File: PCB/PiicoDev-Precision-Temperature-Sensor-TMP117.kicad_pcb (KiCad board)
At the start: 2 copper layers, 25.4 x 25.4 mm, 23 parts, among them J1 , J2 , J3 , U1 TMP117

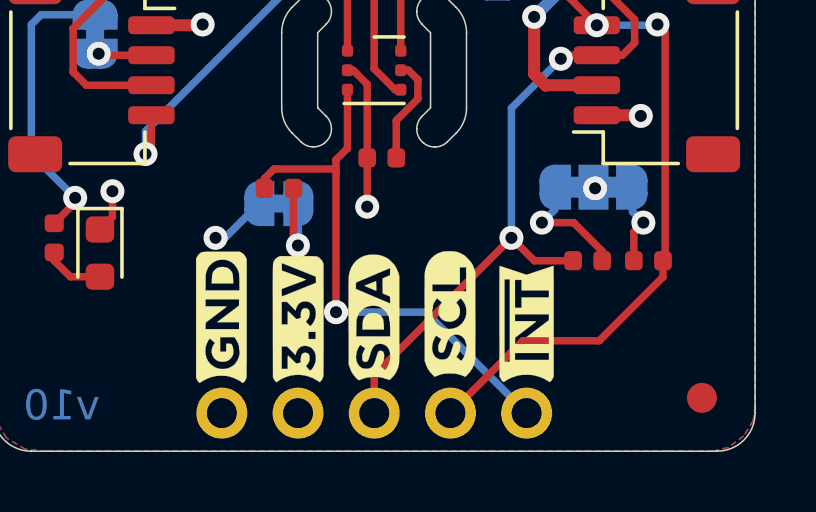
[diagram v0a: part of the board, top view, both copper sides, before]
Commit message: Update R1 to 4k7
New LED is more efficient, use larger resistor. Optimise 1k out of the BOM
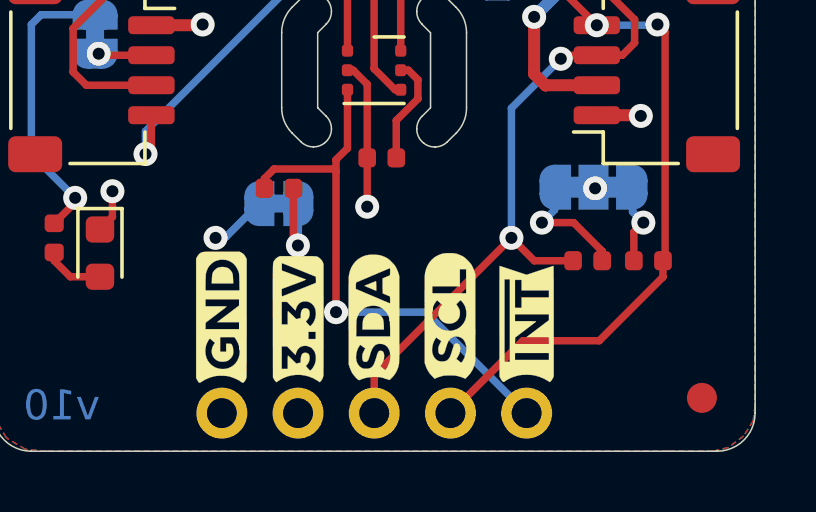
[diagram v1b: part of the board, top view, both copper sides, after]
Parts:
- R1: value 1k -> 4k7

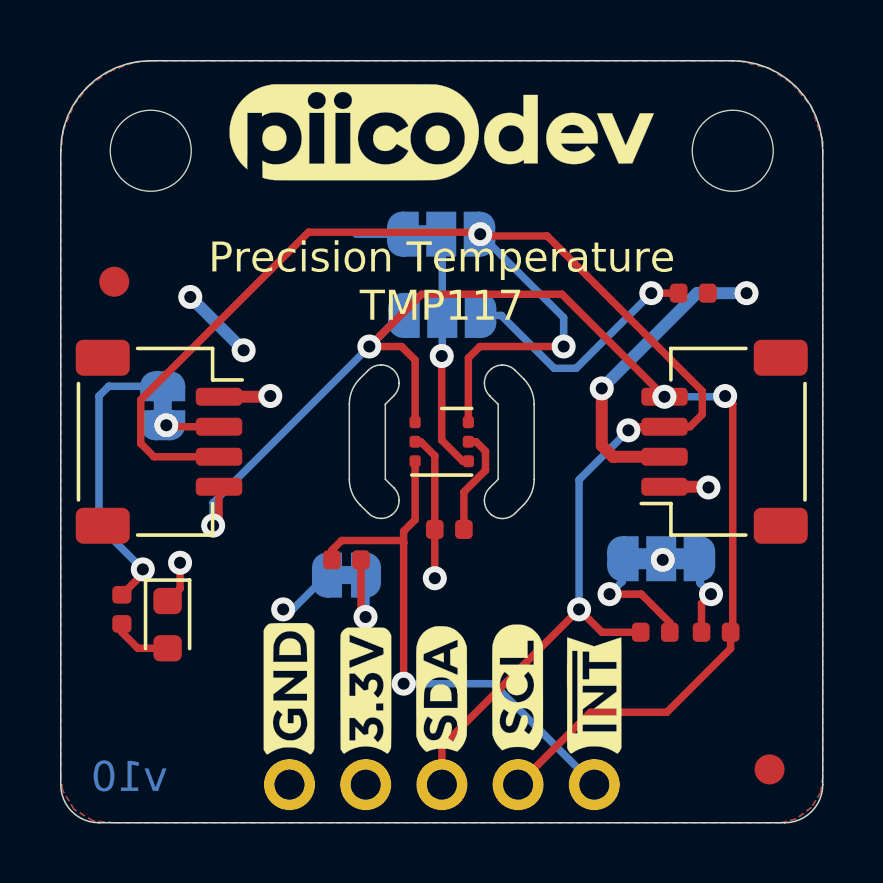
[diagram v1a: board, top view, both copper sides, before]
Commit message: v11 Update
Change resistor values
Add DIP switch and remove ADR jumper
Update graphic labels
Remove solder mask between jumper pads
Update text formatting
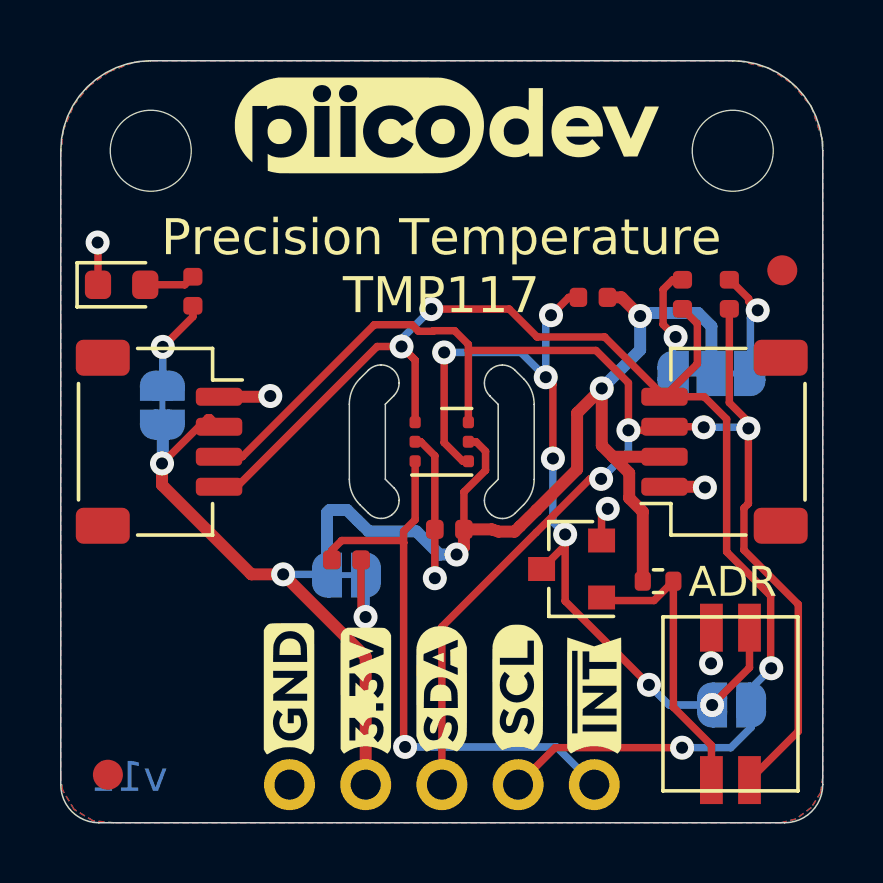
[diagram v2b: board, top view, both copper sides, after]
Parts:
- removed JP5: , Jumper:SolderJumper-3_P1.3mm_Bridged12_RoundedPad1.0x1.5mm
- added G3: LOGO_made-with-love, CoreElectronics_Artwork:piicodev_logo_14.2x3.4mm, B.Cu at (12.6, 2.27)
- added Q1: BSS138, Package_TO_SOT_SMD:SOT-23, F.Cu at (17.0, 16.9)
- added R6: 10k, Resistor_SMD:R_0402_1005Metric, F.Cu at (19.9, 17.3)
- added SW1: SW_DIP_x02, CoreElectronics_Components:SW_DIP_x02_Slide_CHS-02A1, F.Cu at (22.3, 21.4)
- G1: value LOGO_CoreElectronics_made-with-love -> LOGO_CoreElectronics_no-text; footprint PiicoDev_Artwork:piicodev_logo_14.2x3.4mm -> CoreElectronics_Artwork:CoreElectronics_logo_5mm
- G2: footprint Piico_Artwork:piicodev_logo_14.2x3.4mm -> CoreElectronics_Artwork:piicodev_logo_14.2x3.4mm
- JP1, JP2: footprint Jumper:SolderJumper-2_P1.3mm_Bridged_RoundedPad1.0x1.5mm -> CoreElectronics_Components:SolderJumper-2_P1.3mm_Bridged_RoundedPad1.0x1.5mm
- JP4: value (none) -> SolderJumper_2_Open; footprint Jumper:SolderJumper-3_P1.3mm_Open_RoundedPad1.0x1.5mm -> CoreElectronics_Components:SolderJumper-2_P1.3mm_Open_RoundedPad1.0x1.5mm
- R1, R3, R4: value 4k7 -> 10k
- moved FID1 22.3 mm to (24.1, 6.99)
- moved FID2 22.1 mm to (1.57, 23.8)
- moved G1 19.4 mm to (3.46, 19.6)
- moved JP4 16.2 mm to (22.4, 21.5), turned to 0 degrees
- moved R4 11.5 mm to (22.3, 7.79), turned to 270 degrees
- moved D1 11.4 mm to (2.03, 7.47), turned to 0 degrees
- moved R3 11.3 mm to (20.7, 7.79), turned to 270 degrees
- moved R1 10.9 mm to (4.40, 7.68), turned to 90 degrees
- moved LOGO1 6.42 mm to (22.4, 16.5)
- moved JP3 6.40 mm to (21.7, 10.4), turned to 180 degrees
- moved R5 3.35 mm to (17.7, 7.89)
- moved G2 0.29 mm to (12.9, 2.26)
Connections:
- JP4 pad 1: Net-(JP4-Pad1) -> /ADD0
- JP4 pad 2: /ADD0 -> /SCL
- R5 pad 2: Net-(JP4-Pad1) -> /ADD0
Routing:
- net +3V3: track 20.1 -> 56.0 mm, vias 7 -> 5
- net /ADD0: track 8.07 -> 29.9 mm, vias 1 -> 7
- net Net-(Q1-Pad1): track 0.00 -> 9.86 mm
- net Net-(JP4-Pad1): track 8.35 -> 0.00 mm, vias 1 -> 0
- net Net-(JP1-Pad2): track 9.78 -> 3.10 mm
- net /SDA: track 58.1 -> 56.7 mm
- net /SCL: track 46.4 -> 47.7 mm
- net /~INT: track 18.2 -> 19.4 mm
- net Net-(JP3-Pad3): track 2.73 -> 3.80 mm
- net GND: track 11.1 -> 11.8 mm, vias 4 -> 6
- added copper zone on F.Cu, net (none)
- removed copper zone on F.Cu, net +3V3
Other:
- net class +3V3 added: clearance 0.2, trace_width 0.4, via_dia 0.8, via_drill 0.4
- board text added: "ADR"
- board text added: "ADR3"
- board text added: "v11"
- board text removed: "48"
- board text removed: "49"
- board text removed: "4A"
- board text removed: "4B"
- board text removed: "ADDR"
- board text removed: "v10"

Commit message: v12 Update
Migrate to KiCad 6.0
Add 120R resistor
Add 4-bit DIP SW
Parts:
- removed JP4: SolderJumper_2_Open, CoreElectronics_Components:SolderJumper-2_P1.3mm_Open_RoundedPad1.0x1.5mm
- removed Q1: BSS138, Package_TO_SOT_SMD:SOT-23
- R6: value 10k -> 120R
- SW1: value SW_DIP_x02 -> SW_DIP_x04; footprint CoreElectronics_Components:SW_DIP_x02_Slide_CHS-02A1 -> CoreElectronics_Components:SW_DIP_x04_Slide_CHS-04A1
- moved G1 17.5 mm to (20.9, 21.3)
- moved R6 9.69 mm to (14.0, 9.65)
- moved R5 9.14 mm to (17.3, 17.0)
- moved J3 2.50 mm to (5.13, 24.1)
- moved SW1 1.46 mm to (20.9, 21.6)
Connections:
- net /~INT renamed /~{INT}
- R5 pad 2: /ADD0 -> Net-(SW1-Pad2)
- R6 pad 1: +3V3 -> Net-(R6-Pad1)
- R6 pad 2: Net-(Q1-Pad1) -> /SDA
- SW1 pad 1: Net-(Q1-Pad1) -> GND
- SW1 pad 2: /SDA -> Net-(SW1-Pad2)
- SW1 pad 3: /ADD0 -> Net-(R6-Pad1)
- SW1 pad 4: GND -> /SCL
- U1 pad 4: /ADD0 -> Net-(SW1-Pad5)
- U1 pad 6: /SDA -> Net-(R6-Pad1)
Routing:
- net /ADD0: track 29.9 -> 0.00 mm, vias 7 -> 0
- net Net-(R6-Pad1): track 0.00 -> 24.7 mm, vias 0 -> 4
- net Net-(SW1-Pad5): track 0.00 -> 22.7 mm, vias 0 -> 4
- net /SDA: track 56.7 -> 44.2 mm
- net Net-(Q1-Pad1): track 9.86 -> 0.00 mm
- net Net-(SW1-Pad2): track 0.00 -> 8.53 mm, vias 0 -> 2
- net /SCL: track 47.7 -> 56.2 mm, vias 4 -> 5
- net +3V3: track 56.0 -> 55.0 mm, vias 5 -> 4
- net GND: track 11.8 -> 10.8 mm, vias 6 -> 5
- net /~{INT}: track 19.4 -> 18.6 mm, vias 1 -> 4
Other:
- net class +3V3 removed
- net class Default removed
- board text added: "ASW"
- board text added: "v12"
- board text removed: "ADR"
- board text removed: "ADR3"
- board text removed: "v11"

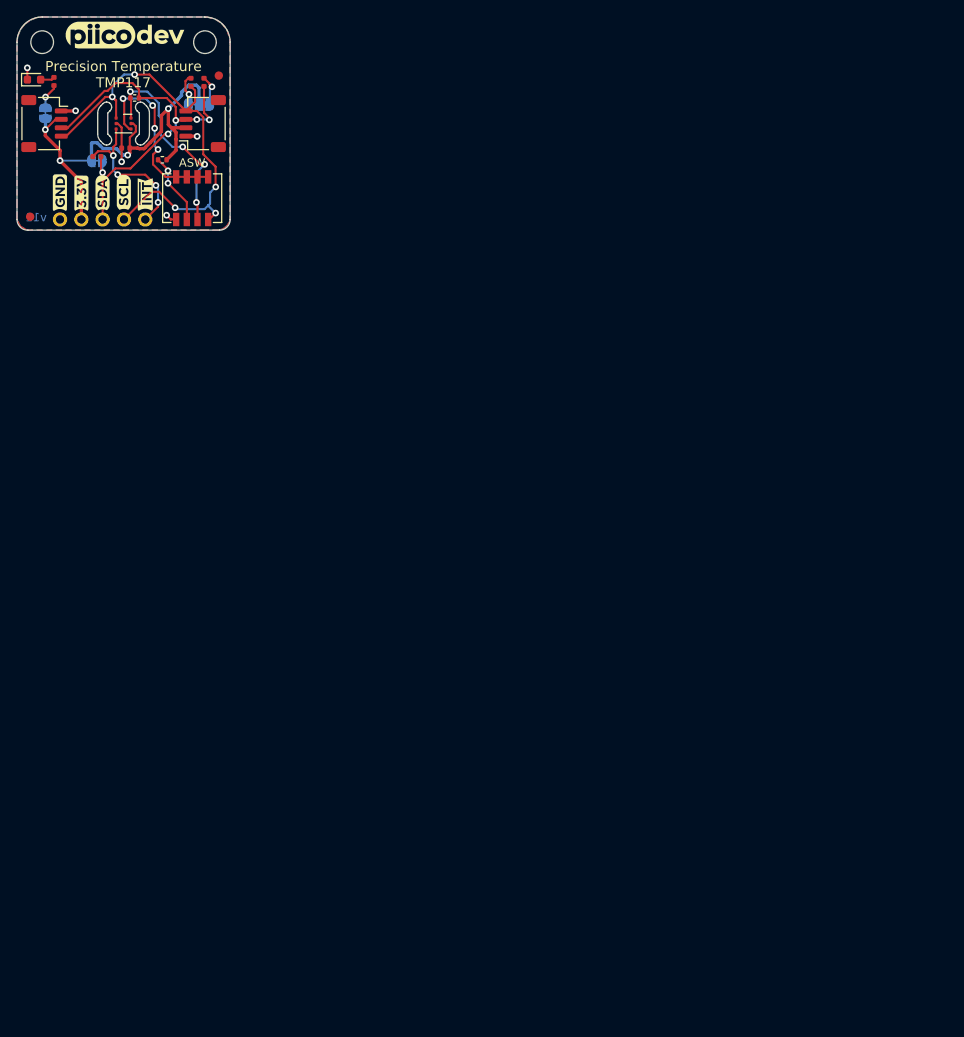
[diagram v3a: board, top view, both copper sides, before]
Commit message: Tweak thermal holes
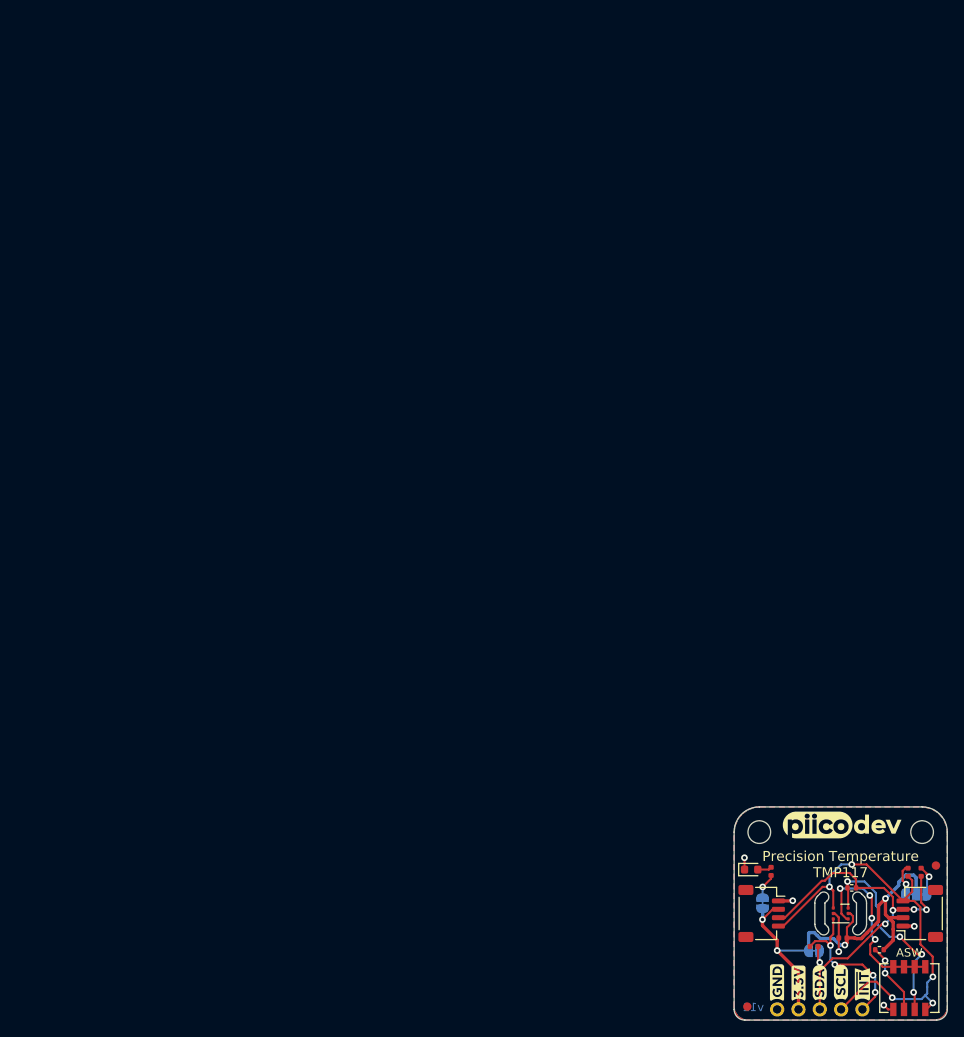
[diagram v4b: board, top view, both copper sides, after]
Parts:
- moved FID1 127.1 mm to (109.5, 101.1)
- moved G2 127.1 mm to (98.3, 96.4)
- moved H1 127.1 mm to (88.5, 97.1)
- moved J1 127.1 mm to (88.7, 106.8)
- moved J3 127.1 mm to (90.6, 118.3)
- moved JP1 127.1 mm to (88.8, 105.6)
- moved JP3 127.1 mm to (107.1, 104.6)
- moved LOGO1 127.1 mm to (107.8, 110.6)
- moved R1 127.1 mm to (89.9, 101.8)
- moved R6 127.1 mm to (99.5, 103.8)
- moved U1 127.1 mm to (98.2, 106.8)
- moved C1 127.1 mm to (98.4, 109.8)
- moved D1 127.1 mm to (87.5, 101.6)
- moved FID2 127.1 mm to (87.0, 117.9)
- moved G1 127.1 mm to (106.3, 115.5)
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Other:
- outline, holes or cut-outs redrawn
